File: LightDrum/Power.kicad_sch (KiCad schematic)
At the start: 61 parts, among them U1001 AP3401, U1002 LM22673-SOIC, U1003 TPS7A94, U701 INA4181 A2, U702 INA4181 A2

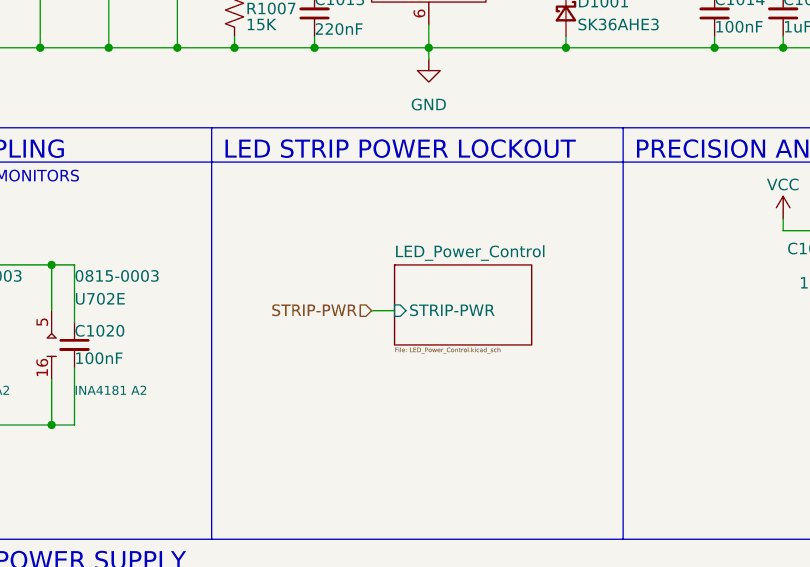
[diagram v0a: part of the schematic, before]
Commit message: Replace relays and SWD conn
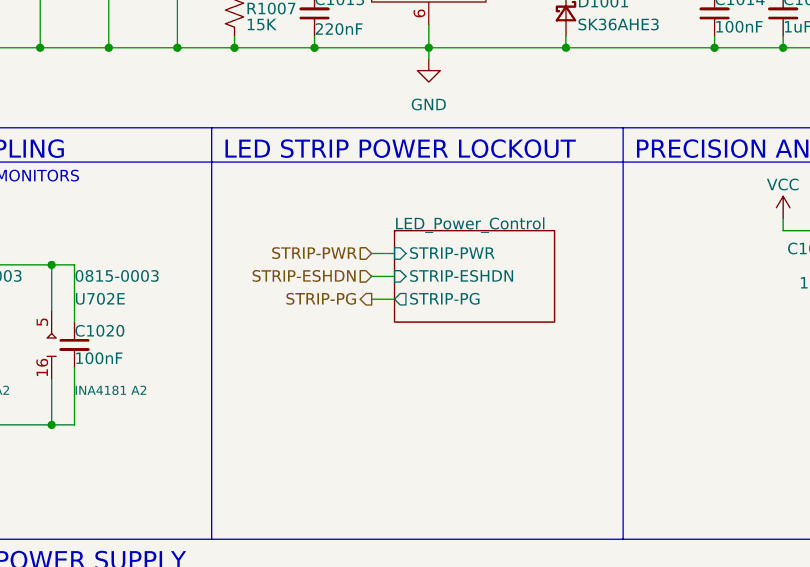
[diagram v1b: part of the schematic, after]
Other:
- sheet LED_Power_Control ports: added STRIP-ESHDN, STRIP-PG; removed none
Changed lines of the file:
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@@
+    (stroke (width 0) (type default))
+  )
+  (wire (pts (xy 69.85 72.39) (xy 72.39 72.39))
     (stroke (width 0) (type default))
   )
@@
     (stroke (width 0) (type default))
   )
+  (wire (pts (xy 69.85 69.85) (xy 72.39 69.85))
+    (stroke (width 0) (type default))
+  )
   (wire (pts (xy 74.93 139.7) (xy 74.93 140.97))
     (stroke (width 0) (type default))
@@
     (stroke (width 0) (type default))
   )
-  (wire (pts (xy 69.85 73.66) (xy 72.39 73.66))
+  (wire (pts (xy 69.85 67.31) (xy 72.39 67.31))
     (stroke (width 0) (type default))
   )
@@
     (effects (font (size 1.27 1.27)) (justify left bottom))
   )
-  (hierarchical_label "STRIP-PWR" (shape input) (at 69.85 73.66 180) (fields_autoplaced)
+  (hierarchical_label "STRIP-PG" (shape output) (at 69.85 72.39 180) (fields_autoplaced)
     (effects (font (size 1.27 1.27)) (justify right))
   )
+  (hierarchical_label "STRIP-PWR" (shape input) (at 69.85 67.31 180) (fields_autoplaced)
+    (effects (font (size 1.27 1.27)) (justify right))
+  )
   (hierarchical_label "VDD-PG" (shape output) (at 176.53 35.56 180) (fields_autoplaced)
+    (effects (font (size 1.27 1.27)) (justify right))
+  )
+  (hierarchical_label "STRIP-ESHDN" (shape input) (at 69.85 69.85 180) (fields_autoplaced)
     (effects (font (size 1.27 1.27)) (justify right))
   )
@@
     )
   )
-  (sheet (at 72.39 68.58) (size 15.24 8.89) (fields_autoplaced)
+  (sheet (at 72.39 64.77) (size 17.78 10.16)
     (stroke (width 0.1524) (type solid))
     (fill (color 0 0 0 0.0000))
-    (property "Sheetname" "LED_Power_Control" (at 72.39 67.8684 0)
+    (property "Sheetname" "LED_Power_Control" (at 72.39 64.77 0)
       (effects (font (size 1.27 1.27)) (justify left bottom))
     )
-    (property "Sheetfile" "LED_Power_Control.kicad_sch" (at 72.39 77.7466 0)
-      (effects (font (size 0.5 0.5)) (justify left top))
-    )
-    (pin "STRIP-PWR" input (at 72.39 73.66 180)
-      (effects (font (size 1.27 1.27)) (justify left))
-    )
+    (property "Sheetfile" "LED_Power_Control.kicad_sch" (at 72.39 74.93 0)
+      (effects (font (size 0.5 0.5)) (justify left top) hide)
+    )
+    (pin "STRIP-PWR" input (at 72.39 67.31 180)
+      (effects (font (size 1.27 1.27)) (justify left))
+    )
+    (pin "STRIP-ESHDN" input (at 72.39 69.85 180)
+      (effects (font (size 1.27 1.27)) (justify left))
+    )
+    (pin "STRIP-PG" output (at 72.39 72.39 180)
+      (effects (font (size 1.27 1.27)) (justify left))
+    )

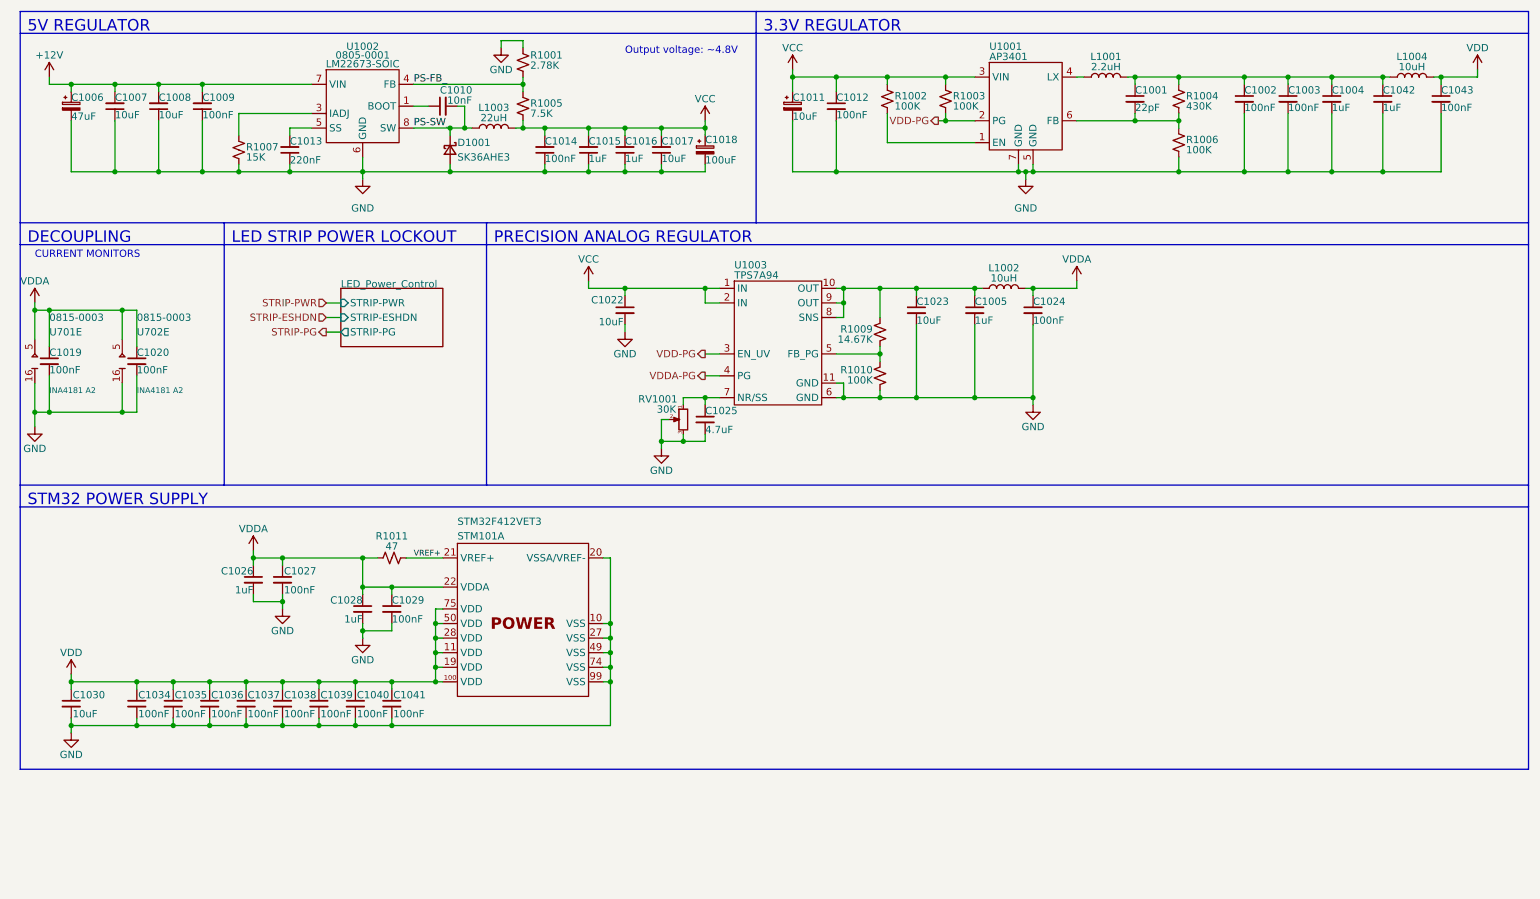
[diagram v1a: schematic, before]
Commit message: Preliminary schematic lock - Starting PCB layout
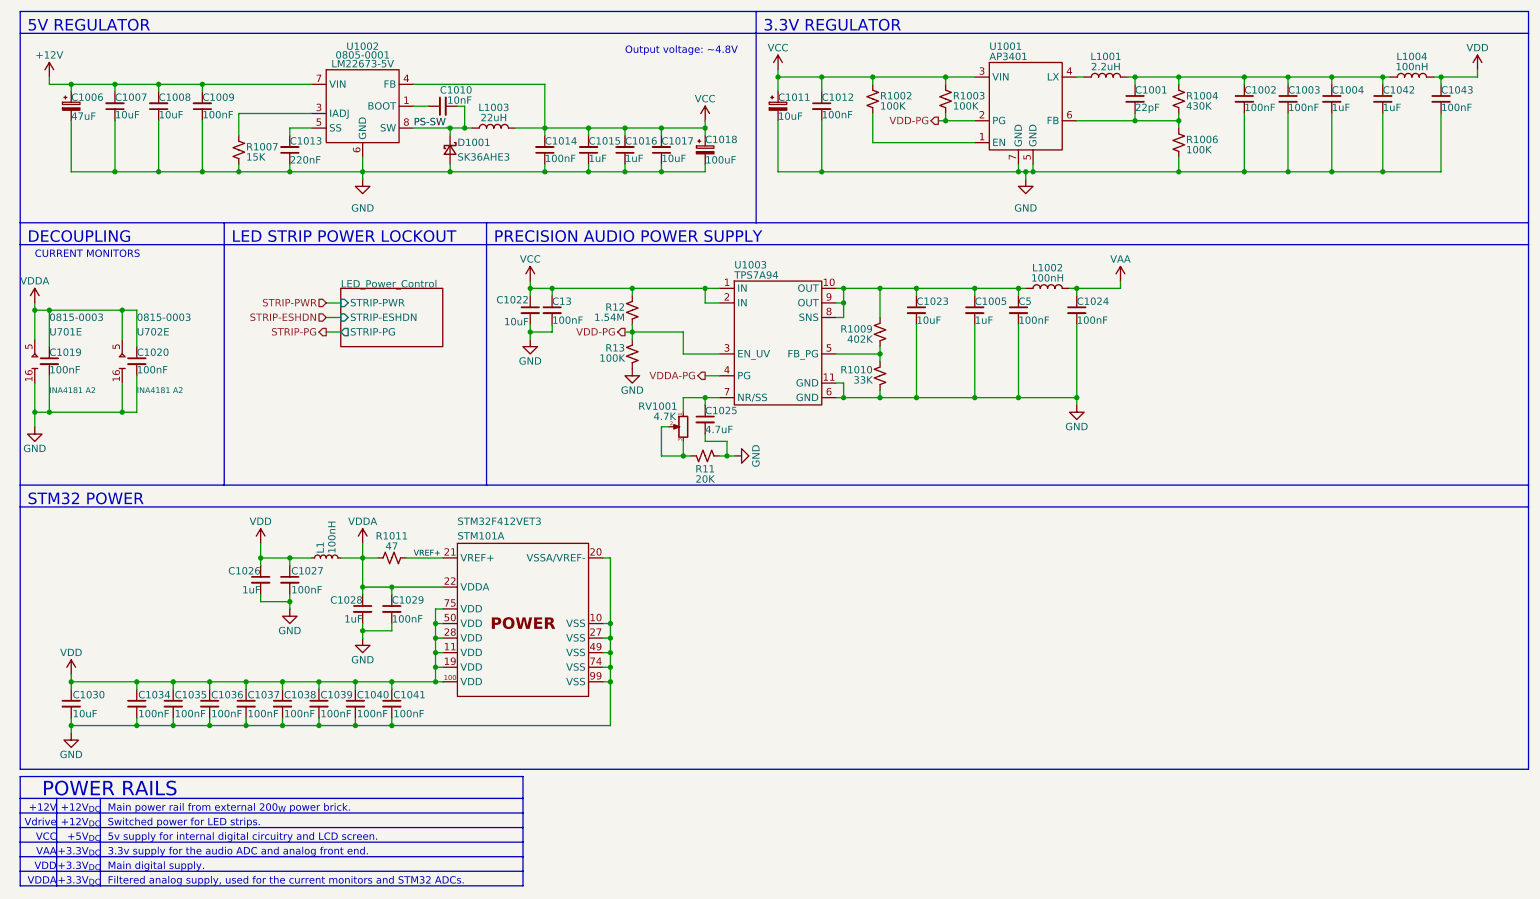
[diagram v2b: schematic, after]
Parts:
- removed R1001: 2.78K, Resistor_SMD:R_0805_2012Metric, symbol Device:R_Small_US
- removed R1005: 7.5K, Resistor_SMD:R_0805_2012Metric, symbol Device:R_Small_US
- added C13, C5: 100nF, Capacitor_SMD:C_0402_1005Metric, symbol Device:C_Small
- added L1: 100nH, Inductor_SMD:L_0603_1608Metric, symbol Daxxn_Device:L
- added R11: 20K, Resistor_SMD:R_0402_1005Metric, symbol Device:R_Small_US
- added R12: 1.54M, Resistor_SMD:R_0402_1005Metric, symbol Device:R_Small_US
- added R13: 100K, Resistor_SMD:R_0402_1005Metric, symbol Device:R_Small_US
- C1001: SupplierPN (none) -> 1276-6849-1-ND
- C1002, C1003, C1009: footprint Capacitor_SMD:C_0805_2012Metric -> Capacitor_SMD:C_0402_1005Metric; SupplierPN (none) -> 1276-1043-1-ND
- C1004, C1005, C1015, C1016, C1026, C1028, C1042: footprint Capacitor_SMD:C_0805_2012Metric -> Capacitor_SMD:C_0603_1608Metric; SupplierPN (none) -> 1276-1102-1-ND
- C1006: SupplierPN (none) -> EMVY500ARA470MF80G
- C1007, C1008, C1017, C1022, C1023, C1030: SupplierPN (none) -> 1276-1854-1-ND
- C1010: footprint Capacitor_SMD:C_0603_1608Metric -> Capacitor_SMD:C_0402_1005Metric; SupplierPN (none) -> 1276-1028-1-ND
- C1011: footprint Capacitor_SMD:CP_Elec_5x5.4 -> Capacitor_SMD:CP_Elec_3x5.4; SupplierPN (none) -> 732-13322-1-ND
- C1012, C1014, C1019, C1020, C1024, C1043: footprint Capacitor_SMD:C_0603_1608Metric -> Capacitor_SMD:C_0402_1005Metric; SupplierPN (none) -> 1276-1043-1-ND
- C1013: footprint Capacitor_SMD:C_0603_1608Metric -> Capacitor_SMD:C_1206_3216Metric; SupplierPN (none) -> 490-GRM31C5C1E224JE02LCT-ND
- C1018: footprint Capacitor_SMD:CP_Elec_6.3x5.4 -> Capacitor_SMD:CP_Elec_6.3x5.2; SupplierPN (none) -> 565-EMVE160ARA101MF55GCT-ND
- C1025: SupplierPN (none) -> 1276-6722-1-ND
- C1027, C1029, C1034, C1035, C1036, C1037, C1038, C1039, C1040, C1041: SupplierPN (none) -> 1276-1043-1-ND
- D1001: SupplierPN (none) -> 353-SK36AHE3-LTPCT-ND
- L1001: SupplierPN (none) -> 490-15950-1-ND
- L1002, L1004: value 10uH -> 100nH; footprint Capacitor_SMD:C_1210_3225Metric -> Inductor_SMD:L_0603_1608Metric; SupplierPN (none) -> 732-6275-1-ND
- L1003: SupplierPN (none) -> 553-4011-1-ND
- R1002, R1003, R1006: SupplierPN (none) -> RMCF0402FT100KCT-ND
- R1004: SupplierPN (none) -> RMCF0402FT430KCT-ND
- R1007: footprint Resistor_SMD:R_0603_1608Metric -> Resistor_SMD:R_0402_1005Metric; SupplierPN (none) -> 2037-PFR05S-153-FNHCT-ND
- R1009: value 14.67K -> 402K; footprint Resistor_SMD:R_0603_1608Metric -> Resistor_SMD:R_0402_1005Metric; SupplierPN (none) -> YAG3151CT-ND
- R1010: value 100K -> 33K; footprint Resistor_SMD:R_0603_1608Metric -> Resistor_SMD:R_0402_1005Metric; SupplierPN (none) -> 311-33.0KLRCT-ND
- R1011: SupplierPN (none) -> 311-47JRCT-ND
- RV1001: value 30K -> 4.7K; SupplierPN (none) -> 118-TC33X-1-472ECT-ND
- STM101: SupplierPN (none) -> 497-18547-ND
- U1001: SupplierPN (none) -> AP3401DNTR-G1DICT-ND
- U1002: value LM22673-SOIC -> LM22673-5V
- U1003: SupplierPN (none) -> 296-TPS7A9401DSCRCT-ND
- U701, U702: SupplierPN (none) -> 296-49082-1-ND
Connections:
- net PS-FB_ is gone; now on net VCC: U1002.4 (FB)
- net GND: now also C13.2, C5.2, R11.2, R13.2; no longer RV1001.2, RV1001.3
- net VCC: now also C13.1, R12.1
- net VDD: now also C1026.1, C1027.1, L1.1
- net VDD-PG: now also R12.2, R13.1
- net VDDA: now also L1.2; no longer C1024.1, C1026.1, C1027.1, L1002.2
- net at C1005.1, C1023.1, L1002.1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: now also C5.1
- new net: R11.1, RV1001.2, RV1001.3
- new net VAA: C1024.1, L1002.2
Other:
- note added: "+12V"
- note added: "+12V_{DC}"
- note added: "+3.3V_{DC}"
- note added: "+5V_{DC}"
- note added: "3.3v supply for the audio ADC and analog front end."
- note added: "5v supply for internal digital circuitry and LCD screen."
- note added: "Filtered analog supply, used for the current monitors and STM32 ADCs."
- note added: "Main digital supply."
- note added: "Main power rail from external 200_{W} power brick."
- note added: "POWER RAILS"
- note added: "PRECISION AUDIO POWER SUPPLY"
- note added: "STM32 POWER"
- note added: "Switched power for LED strips."
- note added: "VAA"
- note added: "VCC"
- note added: "VDD"
- note added: "VDDA"
- note added: "Vdrive"
- note removed: "PRECISION ANALOG REGULATOR"
- note removed: "STM32 POWER SUPPLY"
- moved on the sheet: C1011, C1012, C1022, C1024, C1026, C1027, L1002, R1002, RV1001

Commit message: Component placement complete
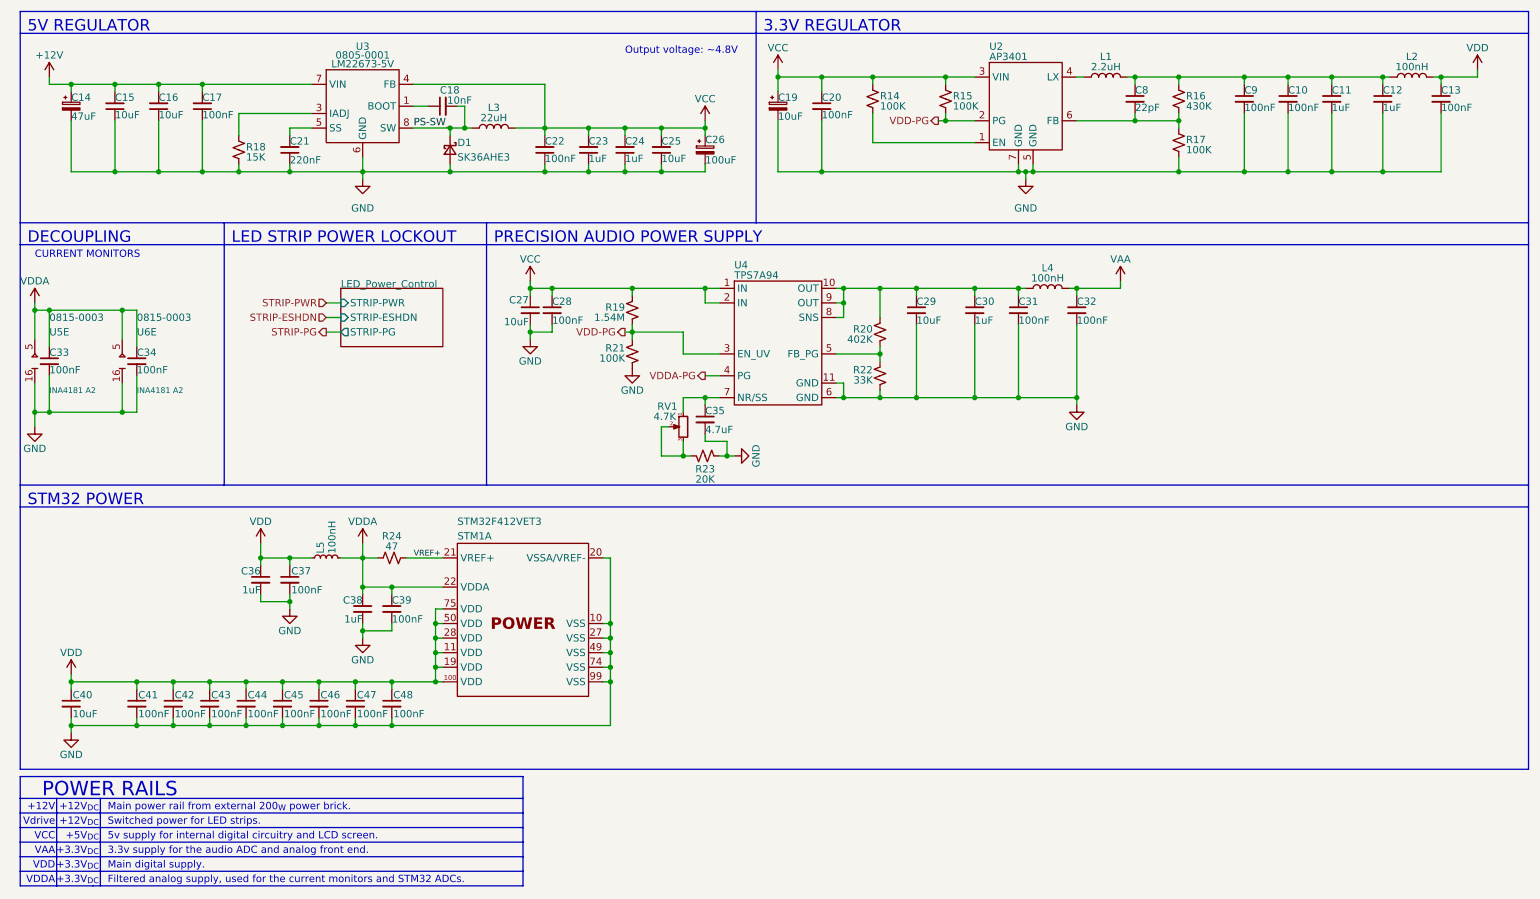
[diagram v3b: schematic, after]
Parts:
- renumbered C1003 to C10, C1004 to C11, C1042 to C12, C1043 to C13, C1006 to C14, C1007 to C15, C1008 to C16, C1009 to C17, C1010 to C18, C1011 to C19, C1012 to C20, C1013 to C21, C1014 to C22, C1015 to C23, C1016 to C24, C1017 to C25, C1018 to C26, C1022 to C27, C13 to C28, C1023 to C29, C1005 to C30, C5 to C31, C1024 to C32, C1019 to C33, C1020 to C34, C1025 to C35, C1026 to C36, C1027 to C37, C1028 to C38, C1029 to C39, C1030 to C40, C1034 to C41, C1035 to C42, C1036 to C43, C1037 to C44, C1038 to C45, C1039 to C46, C1040 to C47, C1041 to C48, C1001 to C8, C1002 to C9, D1001 to D1, L1001 to L1, L1004 to L2, L1003 to L3, L1002 to L4, L1 to L5, R1002 to R14, R1003 to R15, R1004 to R16, R1006 to R17, R1007 to R18, R12 to R19, R1009 to R20, R13 to R21, R1010 to R22, R11 to R23, R1011 to R24, RV1001 to RV1, STM101 to STM1, U1001 to U2, U1002 to U3, U1003 to U4, U701 to U5, U702 to U6

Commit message: First draft layout almost complete
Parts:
- L2: footprint Inductor_SMD:L_0603_1608Metric -> Inductor_SMD:L_1210_3225Metric; SupplierPN 732-6275-1-ND -> NLCV32T-R10M-EFR
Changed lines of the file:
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@@
       (effects (font (size 1.27 1.27)))
     )
-    (property "Footprint" "Inductor_SMD:L_0603_1608Metric" (at 259.08 27.94 0)
+    (property "Footprint" "Inductor_SMD:L_1210_3225Metric" (at 259.08 27.94 0)
       (effects (font (size 1.27 1.27)) hide)
     )
@@
       (effects (font (size 1.27 1.27)) hide)
     )
-    (property "SupplierPN" "732-6275-1-ND" (at 259.08 27.94 0)
-      (effects (font (size 1.27 1.27)) hide)
+    (property "SupplierPN" "NLCV32T-R10M-EFR" (at 259.08 27.94 0)
+      (effects (font (size 1.27 1.27)) hide)
+    )
+    (property "Schematic" "" (at 259.08 27.94 0)
+      (effects (font (size 1.27 1.27)) hide)
+    )
+    (property "PartNumber" "" (at 259.08 27.94 0)
+      (effects (font (size 1.27 1.27)))
     )
     (pin "1")
@@
     (pin "38")
     (pin "39")
-    (pin "4" (alternate "TIM9-CH1"))
+    (pin "4")
     (pin "40")
     (pin "41")
@@
     (pin "65" (alternate "TIM3-CH3"))
     (pin "66" (alternate "TIM3-CH4"))
-    (pin "67")
+    (pin "67" (alternate "TIM1-CH1"))
     (pin "68" (alternate "USART1-TX"))
     (pin "69" (alternate "USART1-RX"))

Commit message: PCB Lock REV11
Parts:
- STM1: footprint Package_QFP:LQFP-100_14x14mm_P0.5mm -> Daxxn_Packages:LQFP-100_14x14mm_P0.5mm
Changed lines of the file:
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@@
       (effects (font (size 1.27 1.27)) (justify left))
     )
-    (property "Footprint" "Package_QFP:LQFP-100_14x14mm_P0.5mm" (at 92.71 102.87 0)
+    (property "Footprint" "Daxxn_Packages:LQFP-100_14x14mm_P0.5mm" (at 92.71 102.87 0)
       (effects (font (size 1.27 1.27)) (justify left) hide)
     )

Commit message: Minor fixes and cleanup - REV11
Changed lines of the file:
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@@
       (effects (font (size 1.27 1.27)) (justify left))
     )
-    (property "Value" "INA4181 A2" (at 21.59 82.55 0)
+    (property "Value" "INA4181 A2" (at 21.59 81.28 0)
       (effects (font (size 1 1)) (justify left))
     )
@@
     )
     (property "PartNumber" "0815-0003" (at 21.59 69.85 0)
-      (effects (font (size 1.27 1.27)) (justify left))
+      (effects (font (size 1.27 1.27)) (justify left) hide)
     )
     (property "SupplierPN" "296-49082-1-ND" (at 19.05 77.47 0)
@@
       (effects (font (size 1.27 1.27)) (justify left))
     )
-    (property "Value" "INA4181 A2" (at 36.83 82.55 0)
+    (property "Value" "INA4181 A2" (at 36.83 81.28 0)
       (effects (font (size 1 1)) (justify left))
     )
@@
     )
     (property "PartNumber" "0815-0003" (at 36.83 69.85 0)
-      (effects (font (size 1.27 1.27)) (justify left))
+      (effects (font (size 1.27 1.27)) (justify left) hide)
     )
     (property "SupplierPN" "296-49082-1-ND" (at 34.29 77.47 0)

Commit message: Replace DSub with much better ECU conn
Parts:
- U2: footprint Package_DFN_QFN:DFN-6-1EP_2x2mm_P0.65mm_EP1x1.6mm -> Daxxn_Packages:DFN-6-1EP_2x2mm_P0.65mm_EP1x1.6mm
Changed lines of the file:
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@@
       (effects (font (size 1.27 1.27)) (justify left))
     )
-    (property "Footprint" "Package_DFN_QFN:DFN-6-1EP_2x2mm_P0.65mm_EP1x1.6mm" (at 191.77 19.05 0)
+    (property "Footprint" "Daxxn_Packages:DFN-6-1EP_2x2mm_P0.65mm_EP1x1.6mm" (at 191.77 19.05 0)
       (effects (font (size 1.27 1.27)) hide)
     )
@@
     (property "SupplierPN" "AP3401DNTR-G1DICT-ND" (at 185.42 25.4 0)
       (effects (font (size 1.27 1.27)) hide)
+    )
+    (property "Schematic" "" (at 185.42 25.4 0)
+      (effects (font (size 1.27 1.27)) hide)
+    )
+    (property "PartNumber" "" (at 185.42 25.4 0)
+      (effects (font (size 1.27 1.27)))
     )
     (pin "1")
@@
     (pin "73")
     (pin "94")
-    (pin "1")
+    (pin "1" (alternate "SPI4-SCK"))
     (pin "15")
     (pin "16")
@@
     (pin "18")
     (pin "2")
-    (pin "23" (alternate "TIM2-CH1"))
-    (pin "24" (alternate "TIM2-CH2"))
+    (pin "23" (alternate "ADC-0"))
+    (pin "24")
     (pin "25" (alternate "USART2-TX"))
     (pin "26" (alternate "USART2-RX"))
@@
     (pin "39")
     (pin "4")
-    (pin "40")
+    (pin "40" (alternate "TIM1-CH1"))
     (pin "41")
-    (pin "42")
-    (pin "43" (alternate "SPI4-SCK"))
-    (pin "44")
-    (pin "45")
+    (pin "42" (alternate "I2S5-WS"))
+    (pin "43" (alternate "I2S5-CK"))
+    (pin "44" (alternate "TIM1-CH3"))
+    (pin "45" (alternate "I2S5-SD"))
     (pin "46")
     (pin "47" (alternate "USART3-TX"))
@@
     (pin "72" (alternate "SWDIO"))
     (pin "76" (alternate "SWCLK"))
-    (pin "77" (alternate "I2S3-WS"))
-    (pin "78" (alternate "I2S3-CK"))
+    (pin "77")
+    (pin "78")
     (pin "79" (alternate "USART3-RX"))
     (pin "8" (alternate "OSC32-IN"))
@@
     (pin "85")
     (pin "86")
-    (pin "87" (alternate "I2S3-SD"))
+    (pin "87")
     (pin "88")
     (pin "89" (alternate "SWO"))
